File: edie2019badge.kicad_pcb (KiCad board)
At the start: 2 copper layers, 90 x 95.7 mm, 27 parts, among them IC1 ESP-32-WROOM

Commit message: added breakout teeth as a component to schematic
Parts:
- renumbered G*** to SKL666
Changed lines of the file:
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@@
   (general
     (thickness 1.6)
-    (drawings 153)
+    (drawings 157)
     (tracks 0)
     (zones 0)
@@
   (module skull:skull locked (layer F.Cu)
     (at 91.3 94.1)
-    (fp_text reference G*** (at 0 0) (layer F.SilkS) hide
+    (fp_text reference SKL666 (at 0 0) (layer F.SilkS) hide
       (effects (font (size 1.524 1.524) (thickness 0.3)))
     )
@@
       (net 67 "Net-(IC1-Pad24)"))
   )
+  (gr_line (start 144.349548 116.055135) (end 140.349548 116.055135) (layer F.Fab) (width 0.2))
+  (gr_line (start 144.349548 113.055135) (end 144.349548 116.055135) (layer F.Fab) (width 0.2))
+  (gr_line (start 140.349548 113.055135) (end 144.349548 113.055135) (layer F.Fab) (width 0.2))
+  (gr_line (start 140.349548 116.055135) (end 140.349548 113.055135) (layer F.Fab) (width 0.2))
   (gr_line (start 81.99658 128.575856) (end 81.460268 127.037771) (layer Edge.Cuts) (width 0.2))
   (gr_line (start 88.094657 138.542403) (end 87.668735 138.068906) (layer Edge.Cuts) (width 0.2))

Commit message: added guesses for uart, i2c and spi pinouts
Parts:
- SKL666: value LOGO -> Skull
- moved D8 2.24 mm to (119.5, 65.7)
- moved D11 1.92 mm to (112.1, 84.3)
- moved D5 1.40 mm to (55.5, 68.9)
- moved D12 1.19 mm to (127.1, 78.5)
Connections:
- net Net-(IC1-Pad29) renamed /esp32/LED_strip_data
- net Net-(IC1-Pad30) renamed /esp32/LED_strip_enable
- IC1 pad 13: Net-(IC1-Pad13) -> /esp32/CLK
- IC1 pad 14: Net-(IC1-Pad14) -> /esp32/MISO
- IC1 pad 16: Net-(IC1-Pad16) -> /esp32/MOSI
- IC1 pad 27: Net-(IC1-Pad27) -> /esp32/RX2
- IC1 pad 28: Net-(IC1-Pad28) -> /esp32/TX2
- IC1 pad 33: Net-(IC1-Pad33) -> /esp32/SDA
- IC1 pad 36: Net-(IC1-Pad36) -> /esp32/SCL
- SKL666 pad 1: (no net) -> GND
- SKL666 pad 2: (no net) -> /esp32/RX2
- SKL666 pad 3: (no net) -> /esp32/TX2
- SKL666 pad 4: (no net) -> /esp32/SCL
- SKL666 pad 5: (no net) -> /esp32/SDA
- SKL666 pad 6: (no net) -> /esp32/MOSI
- SKL666 pad 7: (no net) -> /esp32/MISO
- SKL666 pad 8: (no net) -> /esp32/CLK
- SKL666 pad 9: (no net) -> +5V

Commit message: added shitty add-on headers and changed lanyard hole shape
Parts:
- added CN2: 2x2, pin_headers:2x2, F.Cu at (67.3, 63.6)
- added CN3: 2x2, pin_headers:2x2, F.Cu at (120.3, 106.1)
- added CN4: 2x2, pin_headers:2x2, F.Cu at (63.4, 94.1)
- moved D12 1.41 mm to (126.9, 77.1)
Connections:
- net /esp32/LED_strip_enable renamed /LED strip/LED_strip_enable
- net Net-(IC1-Pad34) renamed /USB interface/RX
- net Net-(IC1-Pad35) renamed /USB interface/TX
- net Net-(IC1-Pad6) renamed /USB interface/USB_power
- IC1 pad 1: Net-(IC1-Pad1) -> GND
- IC1 pad 15: Net-(IC1-Pad15) -> GND
- IC1 pad 29: /esp32/LED_strip_data -> /LED strip/LED_strip_data
- IC1 pad 38: Net-(IC1-Pad38) -> GND
- IC1 pad 39: Net-(IC1-Pad39) -> GND
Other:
- outline, holes or cut-outs redrawn
- net class Default: trace_width 0.25 -> 0.7

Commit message: added voltage regulator
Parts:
- added CN5: 1x6_vertical_sm, pin_headers:1x6_vertical_sm, B.Cu at (72.3, 105.1)
- added IC2: AMS1117-3.3, SOT:SOT-223, B.Cu at (69.3, 87.1)
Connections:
- net +3.3V renamed +3V3
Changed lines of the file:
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@@
     (tracks 0)
     (zones 0)
-    (modules 30)
-    (nets 65)
+    (modules 32)
+    (nets 67)
   )
   (page A4)
@@
     (35 F.Paste user)
     (36 B.SilkS user)
-    (37 F.SilkS user)
+    (37 F.SilkS user hide)
     (38 B.Mask user)
     (39 F.Mask user)
@@
   (net 62 "/USB interface/RX")
   (net 63 "/USB interface/TX")
-  (net 64 +3.3V)
+  (net 64 "Net-(CN5-Pad2)")
+  (net 65 +5V_USB)
+  (net 66 +3V3)
   (net_class Default "This is the default net class."
     (clearance 0.2)
@@
     (uvia_dia 0.3)
     (uvia_drill 0.1)
-    (add_net +3.3V)
+    (add_net +3V3)
     (add_net +5V)
+    (add_net +5V_USB)
     (add_net "/LED strip/+5V_LEDs")
     (add_net "/LED strip/LED_strip_data")
@@
     (add_net /esp32/TX2)
     (add_net GND)
+    (add_net "Net-(CN5-Pad2)")
     (add_net "Net-(D1-Pad1)")
     (add_net "Net-(D10-Pad1)")
@@
     (fp_line (start 1.27 -0.635) (end 1.905 -1.27) (layer F.SilkS) (width 0.15))
     (pad 1 thru_hole roundrect (at 0 0 30) (size 1.524 1.524) (drill 0.762) (layers *.Cu *.Mask) (roundrect_rratio 0.25)
-      (net 64 +3.3V))
+      (net 66 +3V3))
     (pad 2 thru_hole circle (at 2.54 0 30) (size 1.524 1.524) (drill 0.762) (layers *.Cu *.Mask)
       (net 56 /esp32/SDA))
@@
       (net 56 /esp32/SDA))
     (pad 1 thru_hole roundrect (at 0 0) (size 1.524 1.524) (drill 0.762) (layers *.Cu *.Mask) (roundrect_rratio 0.25)
-      (net 64 +3.3V))
+      (net 66 +3V3))
   )
   (module pin_headers:2x2 (layer F.Cu)
@@
     (fp_line (start 1.27 -0.635) (end 1.905 -1.27) (layer F.SilkS) (width 0.15))
     (pad 1 thru_hole roundrect (at 0 0) (size 1.524 1.524) (drill 0.762) (layers *.Cu *.Mask) (roundrect_rratio 0.25)
-      (net 64 +3.3V))
+      (net 66 +3V3))
     (pad 2 thru_hole circle (at 2.54 0) (size 1.524 1.524) (drill 0.762) (layers *.Cu *.Mask)
       (net 56 /esp32/SDA))
@@
       (net 57 /esp32/SCL))
   )
+  (module pin_headers:1x6_vertical_sm (layer B.Cu)
+    (at 72.3 105.1 60)
+    (fp_text reference CN5 (at 0.635 7.62 60) (layer B.SilkS)
+      (effects (font (size 1 1) (thickness 0.15)) (justify mirror))
+    )
+    (fp_text value 1x6_vertical_sm (at 0 5.58 60) (layer B.Fab) hide
+      (effects (font (size 1 1) (thickness 0.15)) (justify mirror))
+    )
+    (fp_line (start 1 6) (end -15 6) (layer B.Fab) (width 0.15))
+    (fp_line (start -15 6) (end -15 -9) (layer B.Fab) (width 0.15))
+    (fp_line (start -15 -9) (end 1 -9) (layer B.Fab) (width 0.15))
+    (fp_line (start 1 -9) (end 1 6) (layer B.Fab) (width 0.15))
+    (fp_poly (pts (xy -13 4) (xy -13 6) (xy -5 6) (xy -5 4)) (layer B.SilkS) (width 0.15))
+    (pad 1 smd rect (at 0 5.08 60) (size 2 1) (layers B.Cu B.Paste B.Mask)
+      (net 28 GND))
+    (pad 2 smd roundrect (at 0 2.54 60) (size 2 1) (layers B.Cu B.Paste B.Mask) (roundrect_rratio 0.25)
+      (net 64 "Net-(CN5-Pad2)"))
+    (pad 3 smd roundrect (at 0 0 60) (size 2 1) (layers B.Cu B.Paste B.Mask) (roundrect_rratio 0.25)
+      (net 65 +5V_USB))
+    (pad 4 smd roundrect (at 0 -2.54 60) (size 2 1) (layers B.Cu B.Paste B.Mask) (roundrect_rratio 0.25)
+      (net 63 "/USB interface/TX"))
+    (pad 5 smd roundrect (at 0 -5.08 60) (size 2 1) (layers B.Cu B.Paste B.Mask) (roundrect_rratio 0.25)
+      (net 62 "/USB interface/RX"))
+    (pad 6 smd roundrect (at 0 -7.62 60) (size 2 1) (layers B.Cu B.Paste B.Mask) (roundrect_rratio 0.25)
+      (net 64 "Net-(CN5-Pad2)"))
+  )
+  (module SOT:SOT-223 (layer B.Cu)
+    (at 69.3 87.1 270)
+    (fp_text reference IC2 (at 0 -0.5 270) (layer B.SilkS) hide
+      (effects (font (size 1 1) (thickness 0.15)) (justify mirror))
+    )
+    (fp_text value AMS1117-3.3 (at 0 0.5 270) (layer B.Fab) hide
+      (effects (font (size 1 1) (thickness 0.15)) (justify mirror))
+    )
+    (fp_line (start 2 2) (end 4 2) (layer B.SilkS) (width 0.15))
+    (fp_line (start 4 -2) (end 3.5 -2) (layer B.SilkS) (width 0.15))
+    (fp_line (start 4 -2) (end 4 2) (layer B.SilkS) (width 0.15))
+    (fp_line (start -2 2) (end -4 2) (layer B.SilkS) (width 0.15))
+    (fp_line (start -4 2) (end -4 -2) (layer B.SilkS) (width 0.15))
+    (fp_line (start -4 -2) (end -3.5 -2) (layer B.SilkS) (width 0.15))
+    (pad 1 smd roundrect (at -2.3 -3.15 270) (size 1.5 2) (layers B.Cu B.Paste B.Mask) (roundrect_rratio 0.25)
+      (net 28 GND))
+    (pad 3 smd roundrect (at 2.3 -3.15 270) (size 1.5 2) (layers B.Cu B.Paste B.Mask) (roundrect_rratio 0.25)
+      (net 58 +5V))
+    (pad 2 smd roundrect (at 0 -3.15 270) (size 1.5 2) (layers B.Cu B.Paste B.Mask) (roundrect_rratio 0.25)
+      (net 66 +3V3))
+    (pad 2 smd roundrect (at 0 3.15 270) (size 3.8 2) (layers B.Cu B.Paste B.Mask) (roundrect_rratio 0.25)
+      (net 66 +3V3))
+  )
   (gr_arc (start 97.3 54.1) (end 97.3 56.1) (angle -180) (layer Edge.Cuts) (width 0.2))

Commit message: added buttons
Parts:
- added SW1: switch_3x6, buttons:sw_3x6, F.Cu at (61.3, 74.1)
- added SW2: switch_3x6, buttons:sw_3x6, F.Cu at (91.3, 71.1)
- added SW3: switch_3x6, buttons:sw_3x6, F.Cu at (121.3, 74.1)
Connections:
- IC1 pad 2: Net-(IC1-Pad2) -> +3V3
- IC1 pad 3: Net-(IC1-Pad3) -> +3V3

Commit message: started doing track layout
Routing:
- net GND: track 0.00 -> 372.4 mm
- net /LED strip/+5V_LEDs: track 0.00 -> 368.3 mm
- net /esp32/SCL: track 0.00 -> 173.4 mm, vias 0 -> 2
- net /esp32/SDA: track 0.00 -> 141.3 mm, vias 0 -> 2
- net Net-(D12-Pad1): track 0.00 -> 90.2 mm
- net Net-(D17-Pad1): track 0.00 -> 77.9 mm
- net Net-(D8-Pad1): track 0.00 -> 76.5 mm
- net /esp32/CLK: track 0.00 -> 73.1 mm, vias 0 -> 1
- net /esp32/MOSI: track 0.00 -> 72.2 mm, vias 0 -> 1
- net /esp32/RX2: track 0.00 -> 69.9 mm, vias 0 -> 1
- net Net-(D4-Pad1): track 0.00 -> 67.2 mm
- net /esp32/MISO: track 0.00 -> 67.2 mm, vias 0 -> 1
- net /esp32/TX2: track 0.00 -> 65.2 mm, vias 0 -> 1
- net Net-(D22-Pad1): track 0.00 -> 54.6 mm
- net Net-(IC1-Pad7): track 0.00 -> 50.3 mm, vias 0 -> 1
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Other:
- net class Default: trace_width 0.7 -> 0.5

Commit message: tweaked trace layout
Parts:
- moved IC2 31.7 mm to (85.4, 114.4)
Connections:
- SKL666 pad 9: +5V -> +3V3
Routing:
- net /esp32/SDA: track 141.3 -> 167.7 mm, vias 2 -> 3
- net /esp32/CLK: track 73.1 -> 64.1 mm
- net Net-(D17-Pad1): track 77.9 -> 84.0 mm
- net /esp32/MISO: track 67.2 -> 64.5 mm
- net /esp32/MOSI: track 72.2 -> 69.8 mm
- net /esp32/SCL: track 173.4 -> 171.3 mm
- net /esp32/RX2: track 69.9 -> 71.2 mm
- net Net-(D8-Pad1): track 76.5 -> 75.6 mm

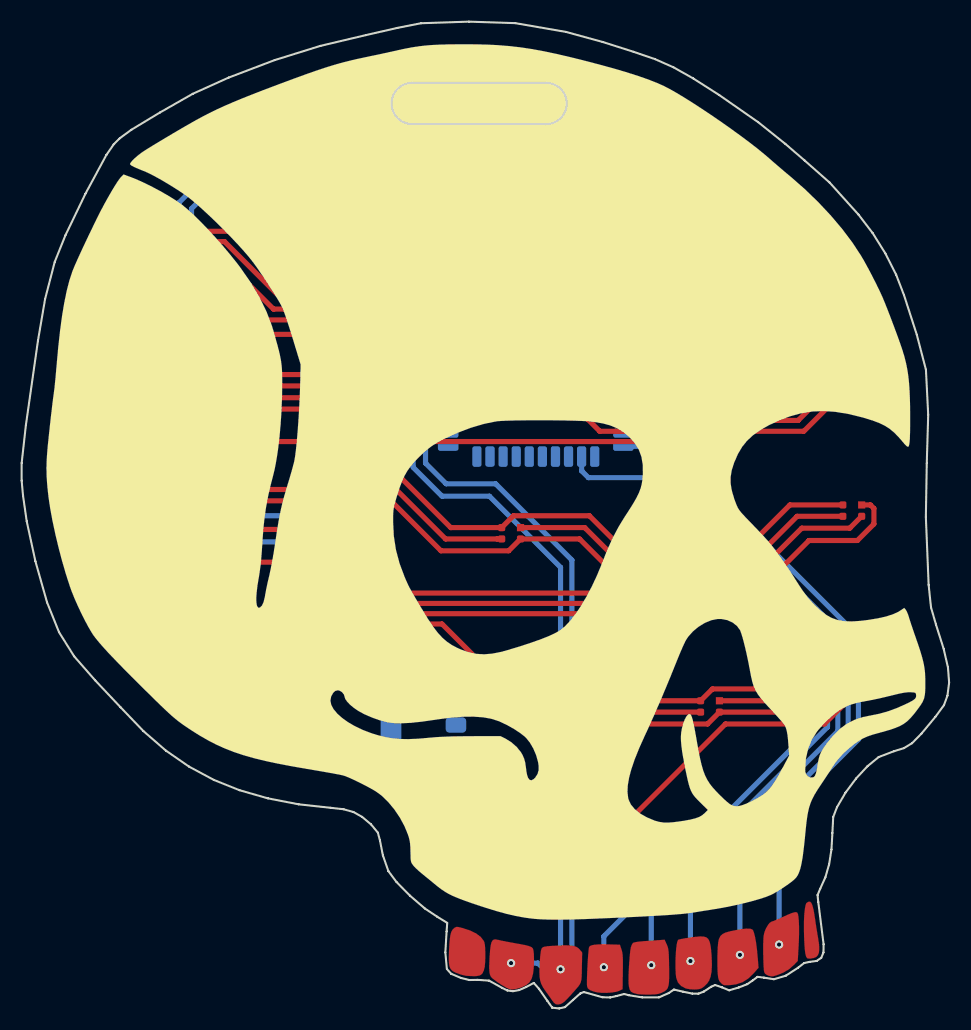
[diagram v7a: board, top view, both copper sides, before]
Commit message: added test points to unused pins
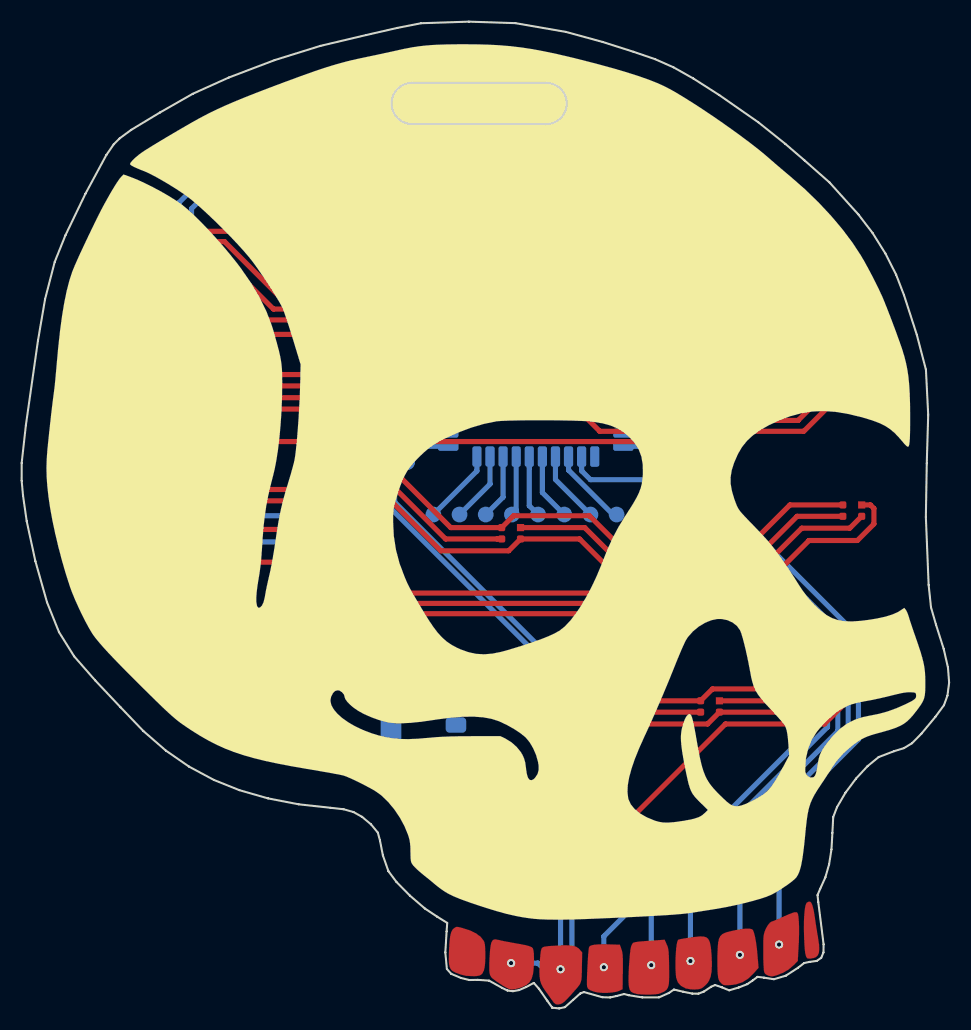
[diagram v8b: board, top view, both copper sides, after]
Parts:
- added TP1: test_point, PCB:test_point, B.Cu at (118.0, 127.0)
- added TP10: test_point, PCB:test_point, B.Cu at (109.2, 81.3)
- added TP11: test_point, PCB:test_point, B.Cu at (109.2, 83.8)
- added TP12: test_point, PCB:test_point, B.Cu at (109.2, 86.4)
- added TP13: test_point, PCB:test_point, B.Cu at (88.9, 94.0)
- added TP14: test_point, PCB:test_point, B.Cu at (86.4, 94.0)
- added TP15: test_point, PCB:test_point, B.Cu at (83.8, 88.9)
- added TP16: test_point, PCB:test_point, B.Cu at (83.8, 86.4)
- added TP17: test_point, PCB:test_point, B.Cu at (83.8, 71.1)
- added TP2: test_point, PCB:test_point, B.Cu at (109.2, 73.7)
- added TP3: test_point, PCB:test_point, B.Cu at (109.2, 76.2)
- added TP4: test_point, PCB:test_point, B.Cu at (104.1, 94.0)
- added TP5: test_point, PCB:test_point, B.Cu at (101.6, 94.0)
- added TP6: test_point, PCB:test_point, B.Cu at (99.1, 94.0)
- added TP7: test_point, PCB:test_point, B.Cu at (96.5, 94.0)
- added TP8: test_point, PCB:test_point, B.Cu at (94.0, 94.0)
- added TP9: test_point, PCB:test_point, B.Cu at (91.4, 94.0)
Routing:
- net Net-(IC1-Pad17): track 0.00 -> 7.77 mm
- net Net-(IC1-Pad24): track 0.00 -> 7.38 mm
- net Net-(IC1-Pad18): track 0.00 -> 7.03 mm
- net Net-(IC1-Pad23): track 0.00 -> 6.85 mm
- net Net-(IC1-Pad19): track 0.00 -> 6.51 mm
- net Net-(IC1-Pad22): track 0.00 -> 6.32 mm
- net Net-(IC1-Pad20): track 0.00 -> 5.98 mm
- net Net-(IC1-Pad21): track 0.00 -> 5.80 mm
- net Net-(IC1-Pad12): track 0.00 -> 5.06 mm
- net Net-(IC1-Pad4): track 0.00 -> 4.83 mm
- net Net-(IC1-Pad10): track 0.00 -> 4.83 mm
- net Net-(IC1-Pad5): track 0.00 -> 4.80 mm
- net Net-(IC1-Pad25): track 0.00 -> 4.62 mm
- net Net-(IC1-Pad11): track 0.00 -> 4.53 mm
- net Net-(IC1-Pad37): track 0.00 -> 4.39 mm
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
